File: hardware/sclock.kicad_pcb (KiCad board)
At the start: 2 copper layers, 40.6 x 23.5 mm, 14 parts, among them J1 Conn_01x04, J2 Conn_01x02, U1 MAX629

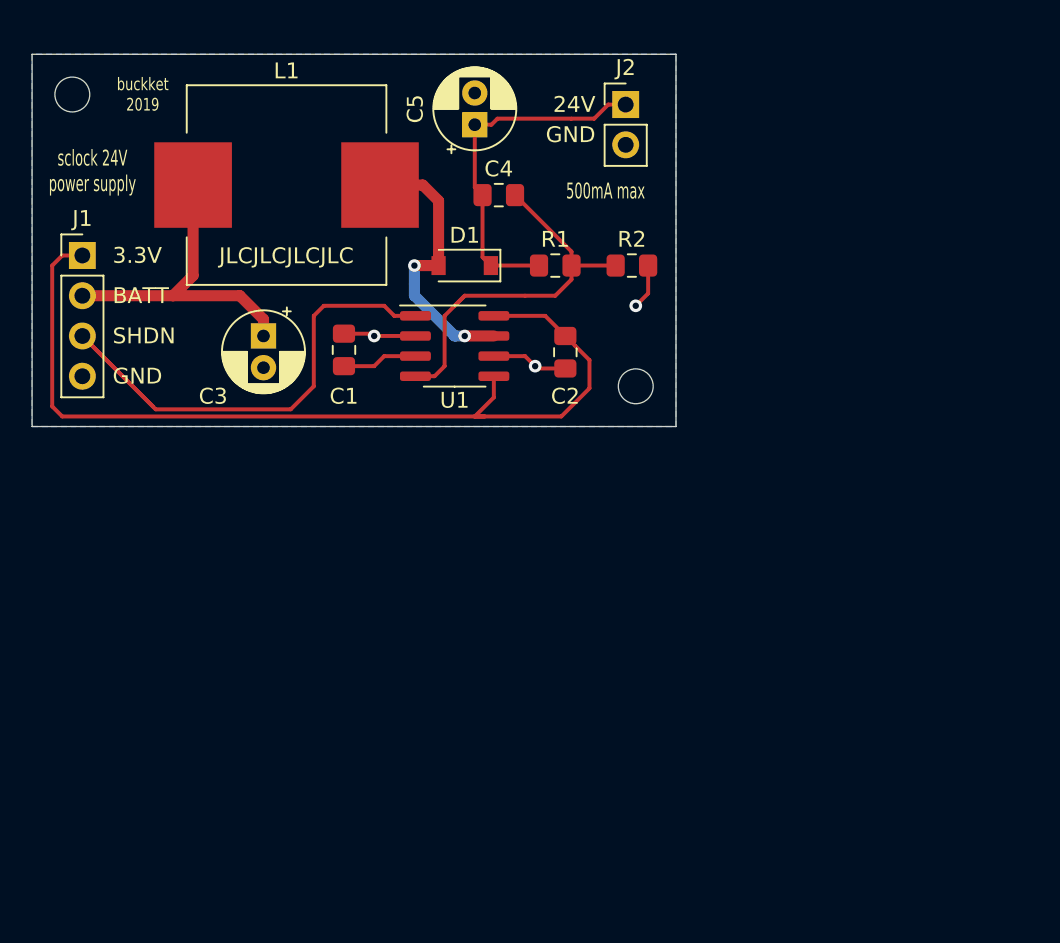
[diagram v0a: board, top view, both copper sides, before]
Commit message: PCB for ATmega328
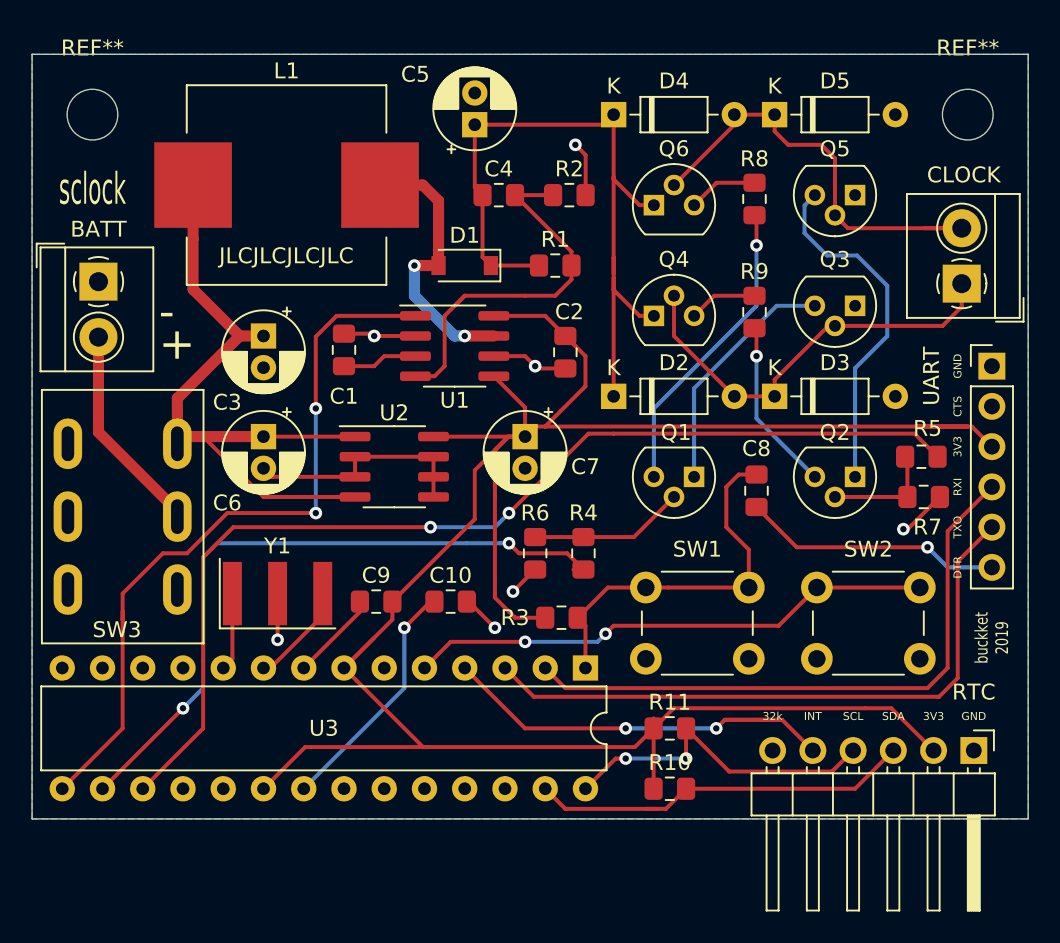
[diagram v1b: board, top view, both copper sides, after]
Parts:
- removed J1: Conn_01x04, Connector_PinHeader_2.54mm:PinHeader_1x04_P2.54mm_Vertical
- removed J2: Conn_01x02, Connector_PinHeader_2.54mm:PinHeader_1x02_P2.54mm_Vertical
- removed the REF** at (103.5, 81.9)
- removed the REF** at (67.9, 63.5)
- added BATT: Conn_Battery, TerminalBlock_4Ucon:TerminalBlock_4Ucon_1x02_P3.50mm_Horizontal, F.Cu at (69.6, 75.3)
- added C10: 0.1uF, Capacitor_SMD:C_0805_2012Metric_Pad1.15x1.40mm_HandSolder, F.Cu at (91.8, 95.5)
- added C6: 10µF, Capacitor_THT:CP_Radial_D5.0mm_P2.00mm, F.Cu at (80.0, 85.1)
- added C7: 10µF, Capacitor_THT:CP_Radial_D5.0mm_P2.00mm, F.Cu at (96.5, 85.1)
- added C8: 0.1uF, Capacitor_SMD:C_0805_2012Metric_Pad1.15x1.40mm_HandSolder, F.Cu at (111.1, 88.5)
- added C9: 0.1uF, Capacitor_SMD:C_0805_2012Metric_Pad1.15x1.40mm_HandSolder, F.Cu at (87.1, 95.5)
- added CLOCK: Conn_Clock, TerminalBlock_4Ucon:TerminalBlock_4Ucon_1x02_P3.50mm_Horizontal, F.Cu at (124.1, 75.4)
- added D2: 1N4148, Diode_THT:D_DO-35_SOD27_P7.62mm_Horizontal, F.Cu at (102.1, 82.5)
- added D3: 1N4148, Diode_THT:D_DO-35_SOD27_P7.62mm_Horizontal, F.Cu at (112.3, 82.5)
- added D4: 1N4148, Diode_THT:D_DO-35_SOD27_P7.62mm_Horizontal, F.Cu at (102.1, 64.8)
- added D5: 1N4148, Diode_THT:D_DO-35_SOD27_P7.62mm_Horizontal, F.Cu at (112.3, 64.8)
- added Q1: KSDC945, Package_TO_SOT_THT:TO-92, F.Cu at (107.2, 87.6)
- added Q2: KSDC945, Package_TO_SOT_THT:TO-92, F.Cu at (117.3, 87.6)
- added Q3: BC63916, Package_TO_SOT_THT:TO-92, F.Cu at (117.3, 76.8)
- added Q4: BC640, Package_TO_SOT_THT:TO-92, F.Cu at (104.6, 77.5)
- added Q5: BC63916, Package_TO_SOT_THT:TO-92, F.Cu at (117.3, 69.8)
- added Q6: BC640, Package_TO_SOT_THT:TO-92, F.Cu at (104.6, 70.5)
- added R10: R, Resistor_SMD:R_0805_2012Metric_Pad1.15x1.40mm_HandSolder, F.Cu at (105.7, 107.3)
- added R11: R, Resistor_SMD:R_0805_2012Metric_Pad1.15x1.40mm_HandSolder, F.Cu at (105.7, 103.5)
- added R3: 10k, Resistor_SMD:R_0805_2012Metric_Pad1.15x1.40mm_HandSolder, F.Cu at (98.8, 96.5)
- added R4: 560, Resistor_SMD:R_0805_2012Metric_Pad1.15x1.40mm_HandSolder, F.Cu at (100.2, 92.5)
- added R5: 560, Resistor_SMD:R_0805_2012Metric_Pad1.15x1.40mm_HandSolder, F.Cu at (121.5, 86.4)
- added R6: 10k, Resistor_SMD:R_0805_2012Metric_Pad1.15x1.40mm_HandSolder, F.Cu at (97.2, 92.5)
- added R7: 10k, Resistor_SMD:R_0805_2012Metric_Pad1.15x1.40mm_HandSolder, F.Cu at (121.7, 88.9)
- added R8: 10k, Resistor_SMD:R_0805_2012Metric_Pad1.15x1.40mm_HandSolder, F.Cu at (111.0, 70.1)
- added R9: 10k, Resistor_SMD:R_0805_2012Metric_Pad1.15x1.40mm_HandSolder, F.Cu at (111.0, 77.2)
- added REF**: MountingHole_3.2mm_M3, MountingHole:MountingHole_3.2mm_M3, F.Cu at (124.5, 64.8)
- added REF**: MountingHole_3.2mm_M3, MountingHole:MountingHole_3.2mm_M3, F.Cu at (69.2, 64.8)
- added RTC: Conn_DS3231, Connector_PinHeader_2.54mm:PinHeader_1x06_P2.54mm_Horizontal, F.Cu at (124.8, 104.9)
- added SW1: Reset, Button_Switch_THT:SW_PUSH_6mm, F.Cu at (104.1, 94.6)
- added SW2: Config, Button_Switch_THT:SW_PUSH_6mm, F.Cu at (114.9, 94.6)
- added SW3: SW_DPDT_x2, sclock:Slide_Switch_DPDT, F.Cu at (74.6, 94.7)
- added U2: MAX604, Package_SO:SOIC-8_3.9x4.9mm_P1.27mm, F.Cu at (88.3, 87.0)
- added U3: ATmega328P-PU, Package_DIP:DIP-28_W7.62mm, F.Cu at (100.3, 99.7)
- added UART: Conn_FTDI, Connector_PinHeader_2.54mm:PinHeader_1x06_P2.54mm_Vertical, F.Cu at (126.0, 80.6)
- added Y1: 8MHz, Crystal:Resonator_SMD_muRata_SFECV-3Pin_6.9x2.9mm, F.Cu at (80.9, 95.0)
- moved R2 5.94 mm to (99.3, 69.8)
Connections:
- net +BATT renamed VCC
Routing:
- net +3V3: track 58.6 -> 149.8 mm
- net CPULSE2: track 0.00 -> 66.4 mm, vias 0 -> 2
- net CPULSE1: track 0.00 -> 42.7 mm, vias 0 -> 2
- net TXO: track 0.00 -> 40.2 mm
- net RXI: track 0.00 -> 39.0 mm
- net Net-(SW2-Pad1): track 0.00 -> 33.4 mm, vias 0 -> 2
- net GND: track 12.3 -> 44.4 mm, vias 3 -> 7
- net VCC: track 20.6 -> 51.2 mm
- net COUT2: track 0.00 -> 28.0 mm
- net INT0: track 0.00 -> 27.9 mm, vias 0 -> 2
- net COUT1: track 0.00 -> 26.7 mm
- net +24V: track 22.4 -> 47.5 mm
- net SDA: track 0.00 -> 24.7 mm
- net Net-(C8-Pad1): track 0.00 -> 24.1 mm
- net Net-(Q2-Pad1): track 0.00 -> 22.2 mm
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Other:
- board size 40.6 x 23.5 mm -> 62.9 x 48.3 mm
- board text added: "+"
- board text added: "-"
- board text added: "32k"
- board text added: "3V3"
- board text added: "CTS"
- board text added: "DTR"
- board text added: "INT"
- board text added: "RXI"
- board text added: "SCL"
- board text added: "SDA"
- board text added: "TXO"
- board text added: "sclock"
- board text removed: "24V"
- board text removed: "3.3V"
- board text removed: "500mA max"
- board text removed: "BATT"
- board text removed: "SHDN"
- board text removed: "sclock 24V power supply"
